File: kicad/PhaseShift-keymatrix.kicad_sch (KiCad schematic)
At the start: 34 parts, among them J1 Conn_01x05, J2 Conn_01x07, J3 Conn_01x07, J4 Conn_01x05, J5 Conn_01x07, J6 Conn_01x07

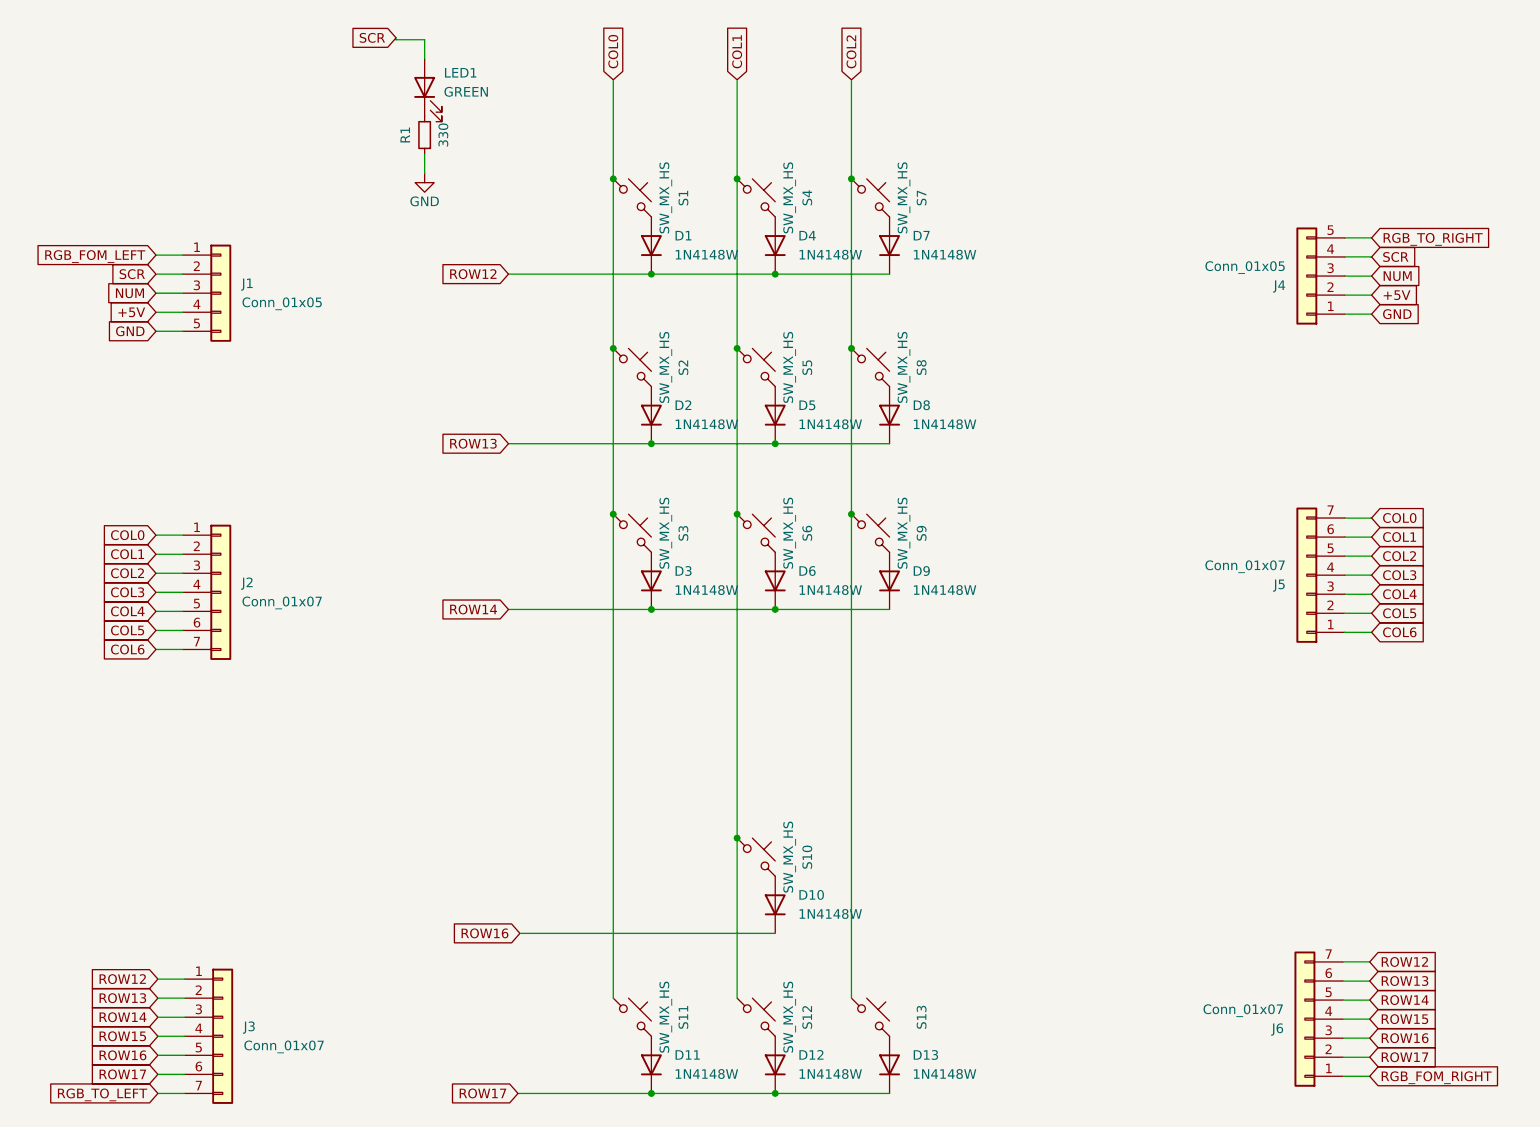
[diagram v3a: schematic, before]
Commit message: artwork for PhaseShift
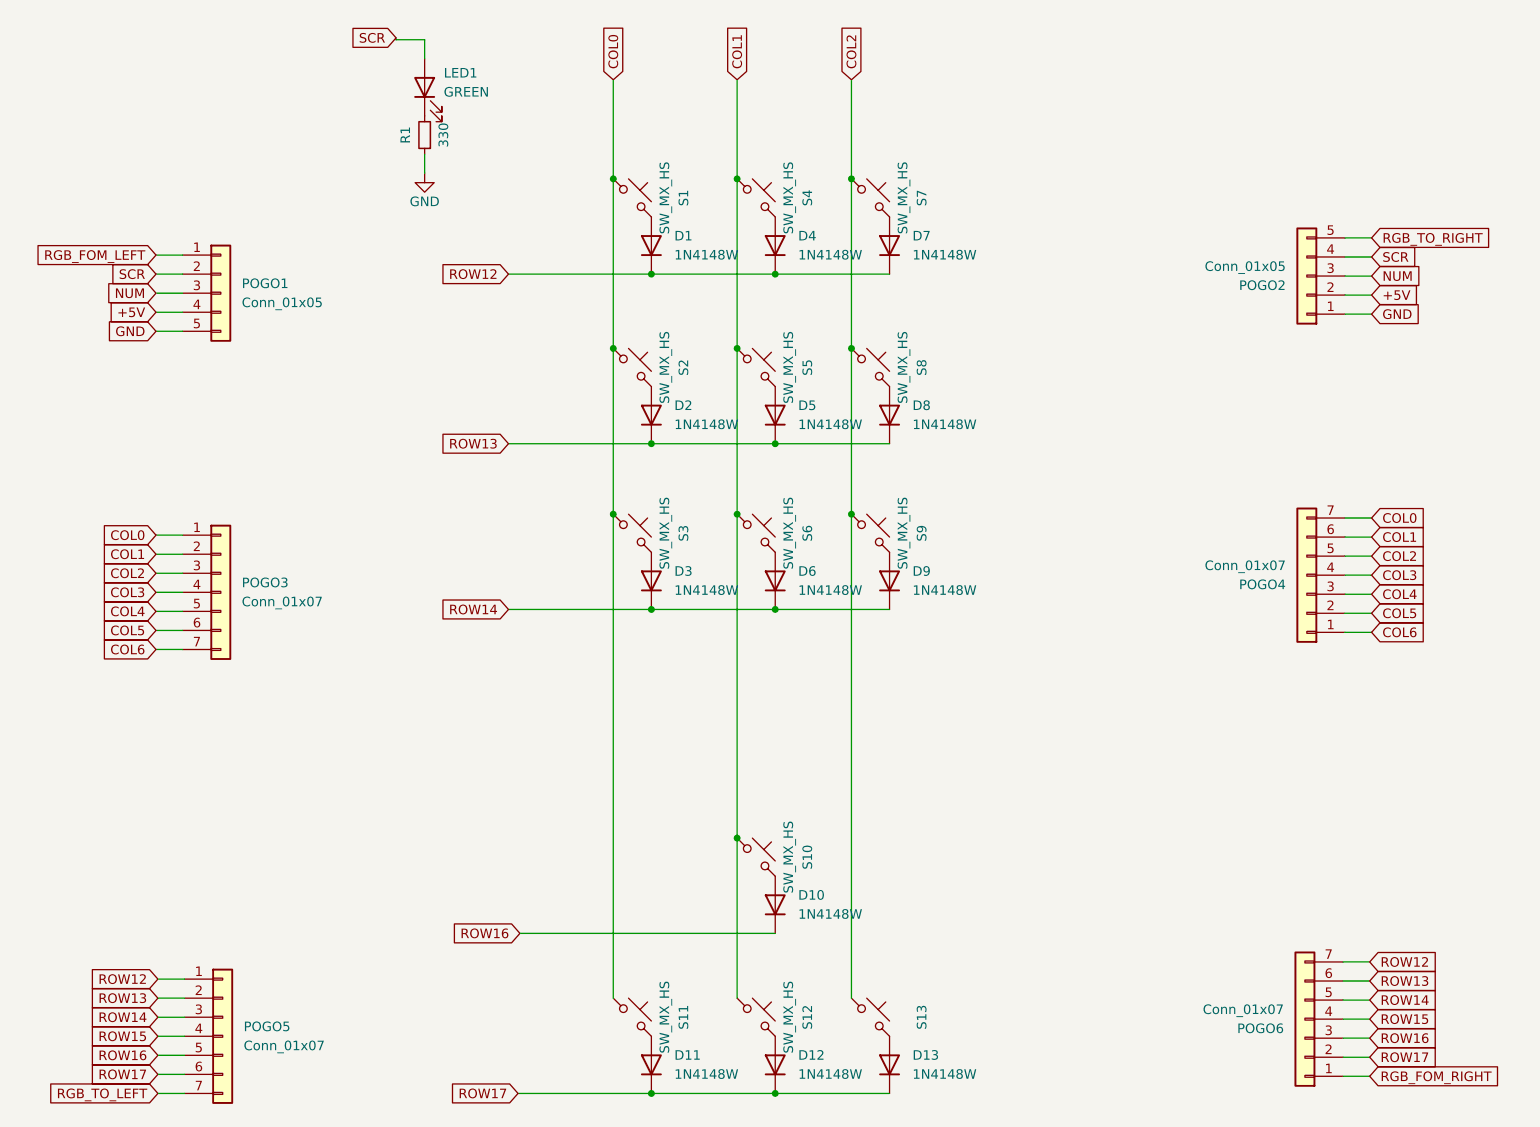
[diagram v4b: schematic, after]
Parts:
- renumbered J1 to POGO1, J4 to POGO2, J2 to POGO3, J5 to POGO4, J3 to POGO5, J6 to POGO6
